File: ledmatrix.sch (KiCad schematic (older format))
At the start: 73 parts

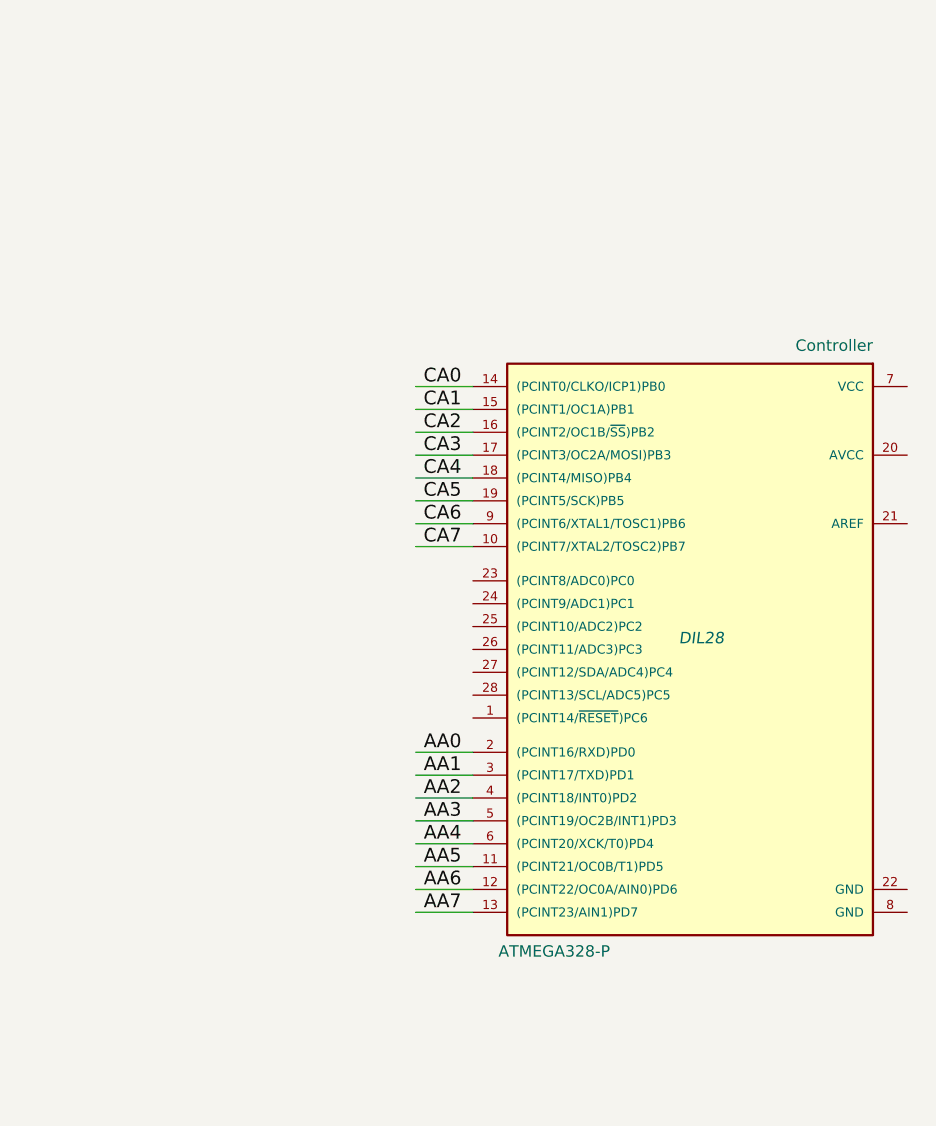
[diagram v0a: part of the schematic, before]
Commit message: added battery
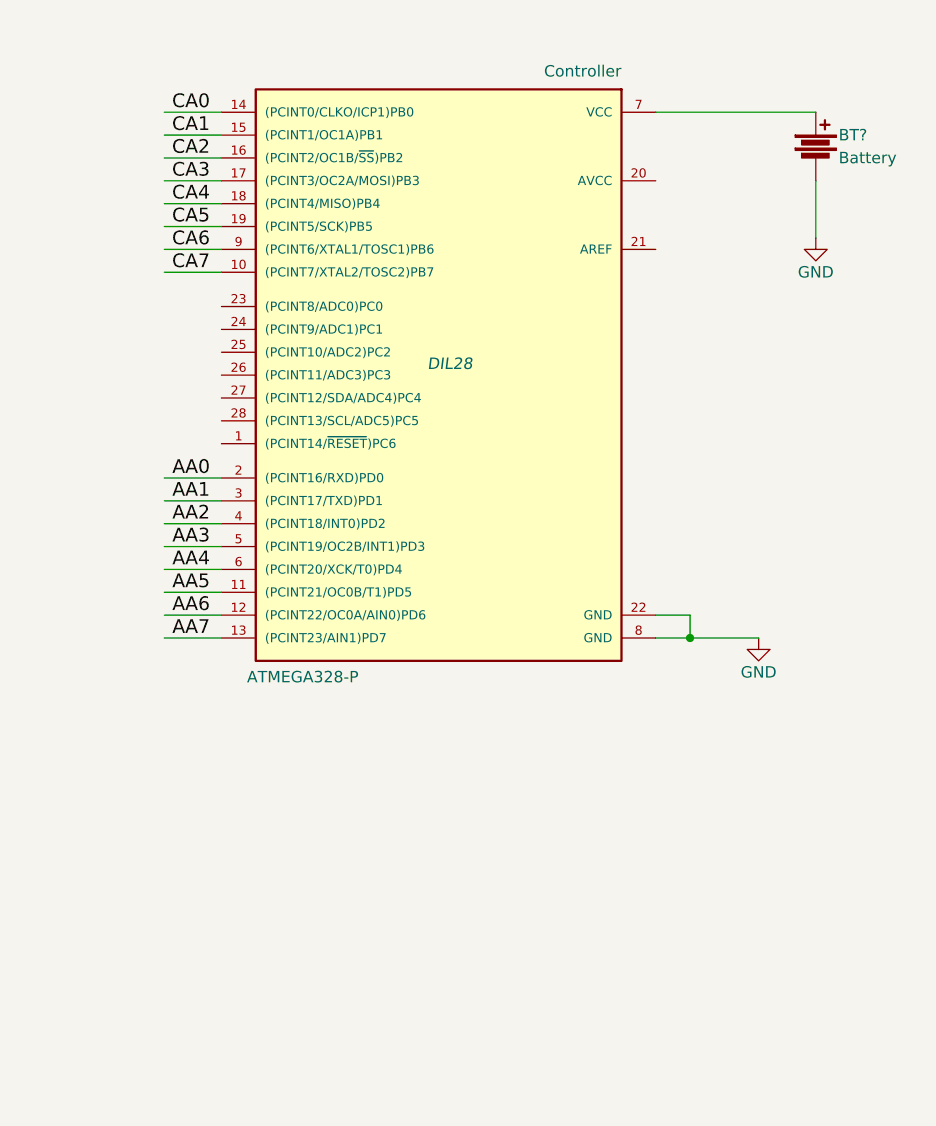
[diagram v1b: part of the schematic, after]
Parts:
- added BT?: Battery, symbol Battery
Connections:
- net labels added: GND
- wire segments 96 -> 101
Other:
- moved on the sheet: Controller
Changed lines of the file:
@@
 LIBS:contrib
 LIBS:valves
+LIBS:ledmatrix-cache
 EELAYER 25 0
 EELAYER END
@@
 L ATMEGA328-P Controller
 U 1 1 5739FEC2
-P 8350 3250
-F 0 "Controller" H 7600 4500 50  0000 L BNN
-F 1 "ATMEGA328-P" H 8750 1850 50  0000 L BNN
-F 2 "DIL28" H 8350 3250 50  0000 C CIN
-F 3 "" H 8350 3250 50  0000 C CNN
-	1    8350 3250
+P 7250 2050
+F 0 "Controller" H 6500 3300 50  0000 L BNN
+F 1 "ATMEGA328-P" H 7650 650 50  0000 L BNN
+F 2 "DIL28" H 7250 2050 50  0000 C CIN
+F 3 "" H 7250 2050 50  0000 C CNN
+	1    7250 2050
 	-1   0    0    -1
 $EndComp
@@
 $EndComp
 Wire Wire Line
-	7350 2150 7100 2150
-Text Label 7300 2150 2    60   ~ 0
+	6250 950  6000 950
+Text Label 6200 950  2    60   ~ 0
 CA0
 Wire Wire Line
-	7350 2250 7100 2250
-Text Label 7300 2250 2    60   ~ 0
+	6250 1050 6000 1050
+Text Label 6200 1050 2    60   ~ 0
 CA1
 Wire Wire Line
-	7350 2350 7100 2350
-Text Label 7300 2350 2    60   ~ 0
+	6250 1150 6000 1150
+Text Label 6200 1150 2    60   ~ 0
 CA2
 Wire Wire Line
-	7350 2450 7100 2450
-Text Label 7300 2450 2    60   ~ 0
+	6250 1250 6000 1250
+Text Label 6200 1250 2    60   ~ 0
 CA3
 Wire Wire Line
-	7350 2550 7100 2550
-Text Label 7300 2550 2    60   ~ 0
+	6250 1350 6000 1350
+Text Label 6200 1350 2    60   ~ 0
 CA4
 Wire Wire Line
-	7350 2650 7100 2650
-Text Label 7300 2650 2    60   ~ 0
+	6250 1450 6000 1450
+Text Label 6200 1450 2    60   ~ 0
 CA5
 Wire Wire Line
-	7350 2750 7100 2750
-Text Label 7300 2750 2    60   ~ 0
+	6250 1550 6000 1550
+Text Label 6200 1550 2    60   ~ 0
 CA6
 Wire Wire Line
-	7350 2850 7100 2850
-Text Label 7300 2850 2    60   ~ 0
+	6250 1650 6000 1650
+Text Label 6200 1650 2    60   ~ 0
 CA7
 Wire Wire Line
@@
 $EndComp
 Wire Wire Line
-	7350 3750 7100 3750
-Text Label 7300 3750 2    60   ~ 0
+	6250 2550 6000 2550
+Text Label 6200 2550 2    60   ~ 0
 AA0
 Wire Wire Line
-	7350 3850 7100 3850
-Text Label 7300 3850 2    60   ~ 0
+	6250 2650 6000 2650
+Text Label 6200 2650 2    60   ~ 0
 AA1
 Wire Wire Line
-	7350 3950 7100 3950
-Text Label 7300 3950 2    60   ~ 0
+	6250 2750 6000 2750
+Text Label 6200 2750 2    60   ~ 0
 AA2
 Wire Wire Line
-	7350 4050 7100 4050
-Text Label 7300 4050 2    60   ~ 0
+	6250 2850 6000 2850
+Text Label 6200 2850 2    60   ~ 0
 AA3
 Wire Wire Line
-	7350 4150 7100 4150
-Text Label 7300 4150 2    60   ~ 0
+	6250 2950 6000 2950
+Text Label 6200 2950 2    60   ~ 0
 AA4
 Wire Wire Line
-	7350 4250 7100 4250
-Text Label 7300 4250 2    60   ~ 0
+	6250 3050 6000 3050
+Text Label 6200 3050 2    60   ~ 0
 AA5
 Wire Wire Line
-	7350 4350 7100 4350
-Text Label 7300 4350 2    60   ~ 0
+	6250 3150 6000 3150
+Text Label 6200 3150 2    60   ~ 0
 AA6
 Wire Wire Line
-	7350 4450 7100 4450
-Text Label 7300 4450 2    60   ~ 0
+	6250 3250 6000 3250
+Text Label 6200 3250 2    60   ~ 0
 AA7
 Wire Wire Line
@@
 Wire Wire Line
 	1600 6950 3900 6950
+$Comp
+L GND #PWR?
+U 1 1 573A1AB7
+P 8600 3250
+F 0 "#PWR?" H 8600 3000 50  0001 C CNN
+F 1 "GND" H 8600 3100 50  0000 C CNN
+F 2 "" H 8600 3250 50  0000 C CNN
+F 3 "" H 8600 3250 50  0000 C CNN
+	1    8600 3250
+	1    0    0    -1
+$EndComp
+Wire Wire Line
+	8150 3250 8600 3250
+Wire Wire Line
+	8150 3150 8300 3150
+Wire Wire Line
+	8300 3150 8300 3250
+Connection ~ 8300 3250
+$Comp
+L Battery BT?
+U 1 1 573A36D4
+P 8850 1100
+F 0 "BT?" H 8950 1150 50  0000 L CNN
+F 1 "Battery" H 8950 1050 50  0000 L CNN
+F 2 "" V 8850 1140 50  0000 C CNN
+F 3 "" V 8850 1140 50  0000 C CNN
+	1    8850 1100
+	1    0    0    -1
+$EndComp
+Wire Wire Line
+	8150 950  8850 950
+Wire Wire Line
+	8850 1250 8850 1500
+$Comp
+L GND #PWR?
+U 1 1 573A3AF4
+P 8850 1500
+F 0 "#PWR?" H 8850 1250 50  0001 C CNN
+F 1 "GND" H 8850 1350 50  0000 C CNN
+F 2 "" H 8850 1500 50  0000 C CNN
+F 3 "" H 8850 1500 50  0000 C CNN
+	1    8850 1500
+	1    0    0    -1
+$EndComp
 $EndSCHEMATC

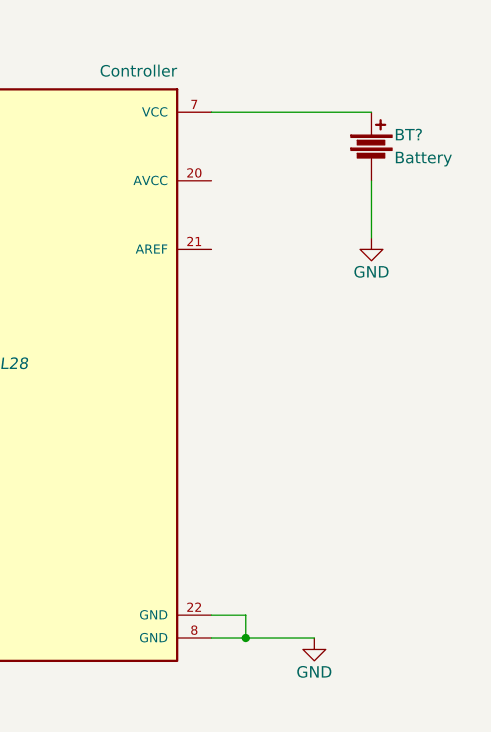
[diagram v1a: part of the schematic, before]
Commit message: Added switch
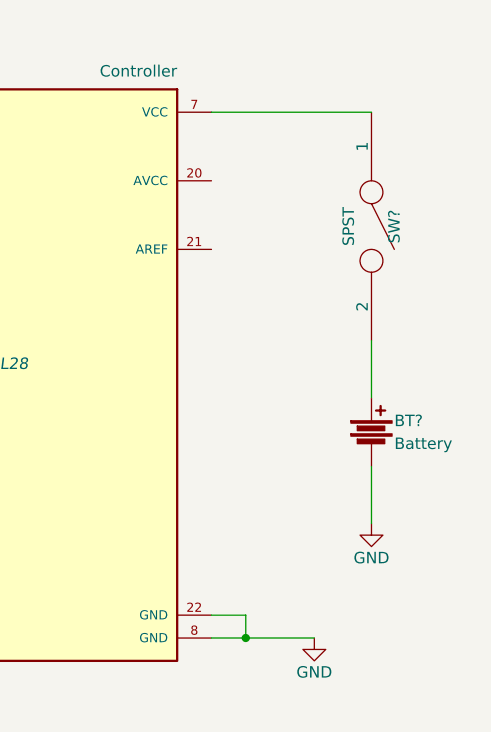
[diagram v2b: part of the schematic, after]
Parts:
- added SW?: SPST, symbol SPST
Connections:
- wire segments 101 -> 102
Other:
- moved on the sheet: BT?
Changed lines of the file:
@@
 L Battery BT?
 U 1 1 573A36D4
-P 8850 1100
-F 0 "BT?" H 8950 1150 50  0000 L CNN
-F 1 "Battery" H 8950 1050 50  0000 L CNN
-F 2 "" V 8850 1140 50  0000 C CNN
-F 3 "" V 8850 1140 50  0000 C CNN
-	1    8850 1100
+P 8850 2350
+F 0 "BT?" H 8950 2400 50  0000 L CNN
+F 1 "Battery" H 8950 2300 50  0000 L CNN
+F 2 "" V 8850 2390 50  0000 C CNN
+F 3 "" V 8850 2390 50  0000 C CNN
+	1    8850 2350
 	1    0    0    -1
 $EndComp
@@
 	8150 950  8850 950
 Wire Wire Line
-	8850 1250 8850 1500
+	8850 2500 8850 2750
 $Comp
 L GND #PWR?
 U 1 1 573A3AF4
-P 8850 1500
-F 0 "#PWR?" H 8850 1250 50  0001 C CNN
-F 1 "GND" H 8850 1350 50  0000 C CNN
-F 2 "" H 8850 1500 50  0000 C CNN
-F 3 "" H 8850 1500 50  0000 C CNN
-	1    8850 1500
+P 8850 2750
+F 0 "#PWR?" H 8850 2500 50  0001 C CNN
+F 1 "GND" H 8850 2600 50  0000 C CNN
+F 2 "" H 8850 2750 50  0000 C CNN
+F 3 "" H 8850 2750 50  0000 C CNN
+	1    8850 2750
 	1    0    0    -1
 $EndComp
+$Comp
+L SPST SW?
+U 1 1 573A441E
+P 8850 1450
+F 0 "SW?" H 8850 1550 50  0000 C CNN
+F 1 "SPST" H 8850 1350 50  0000 C CNN
+F 2 "" H 8850 1450 50  0000 C CNN
+F 3 "" H 8850 1450 50  0000 C CNN
+	1    8850 1450
+	0    1    1    0
+$EndComp
+Wire Wire Line
+	8850 1950 8850 2200
 $EndSCHEMATC

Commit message: Automatic anotation
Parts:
- gave numbers to parts that had none: 74
- renumbered Controller to Controller1
